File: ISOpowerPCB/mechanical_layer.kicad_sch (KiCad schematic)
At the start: 4 parts

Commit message: messing around with libraries
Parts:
- gave numbers to parts that had none: 4
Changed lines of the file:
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@@
   (symbol (lib_id "Mechanical:MountingHole") (at 71.12 78.74 0) (unit 1)
     (in_bom yes) (on_board yes) (fields_autoplaced)
-    (property "Reference" "H?" (id 0) (at 73.66 77.4699 0)
+    (property "Reference" "H4" (id 0) (at 73.66 77.4699 0)
       (effects (font (size 1.27 1.27)) (justify left))
     )
@@
   (symbol (lib_id "Mechanical:MountingHole") (at 71.12 71.12 0) (unit 1)
     (in_bom yes) (on_board yes) (fields_autoplaced)
-    (property "Reference" "H?" (id 0) (at 73.66 69.8499 0)
+    (property "Reference" "H3" (id 0) (at 73.66 69.8499 0)
       (effects (font (size 1.27 1.27)) (justify left))
     )
@@
   (symbol (lib_id "Mechanical:MountingHole") (at 71.12 62.23 0) (unit 1)
     (in_bom yes) (on_board yes) (fields_autoplaced)
-    (property "Reference" "H?" (id 0) (at 73.66 60.9599 0)
+    (property "Reference" "H2" (id 0) (at 73.66 60.9599 0)
       (effects (font (size 1.27 1.27)) (justify left))
     )
@@
   (symbol (lib_id "Mechanical:MountingHole") (at 71.12 53.34 0) (unit 1)
     (in_bom yes) (on_board yes) (fields_autoplaced)
-    (property "Reference" "H?" (id 0) (at 73.66 52.0699 0)
+    (property "Reference" "H1" (id 0) (at 73.66 52.0699 0)
       (effects (font (size 1.27 1.27)) (justify left))
     )

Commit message: Footprint Associations 50% complete
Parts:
- H1, H2, H3, H4: footprint (none) -> MountingHole:MountingHole_3.2mm_M3
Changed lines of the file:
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@@
       (effects (font (size 1.27 1.27)) (justify left))
     )
-    (property "Footprint" "" (id 2) (at 71.12 78.74 0)
+    (property "Footprint" "MountingHole:MountingHole_3.2mm_M3" (id 2) (at 71.12 78.74 0)
       (effects (font (size 1.27 1.27)) hide)
     )
@@
       (effects (font (size 1.27 1.27)) (justify left))
     )
-    (property "Footprint" "" (id 2) (at 71.12 71.12 0)
+    (property "Footprint" "MountingHole:MountingHole_3.2mm_M3" (id 2) (at 71.12 71.12 0)
       (effects (font (size 1.27 1.27)) hide)
     )
@@
       (effects (font (size 1.27 1.27)) (justify left))
     )
-    (property "Footprint" "" (id 2) (at 71.12 62.23 0)
+    (property "Footprint" "MountingHole:MountingHole_3.2mm_M3" (id 2) (at 71.12 62.23 0)
       (effects (font (size 1.27 1.27)) hide)
     )
@@
       (effects (font (size 1.27 1.27)) (justify left))
     )
-    (property "Footprint" "" (id 2) (at 71.12 53.34 0)
+    (property "Footprint" "MountingHole:MountingHole_3.2mm_M3" (id 2) (at 71.12 53.34 0)
       (effects (font (size 1.27 1.27)) hide)
     )

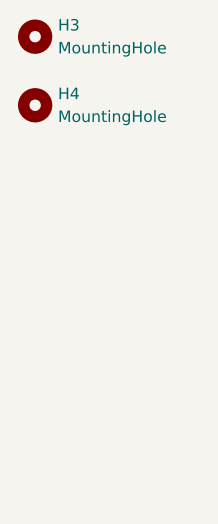
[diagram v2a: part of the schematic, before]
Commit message: Components placed V1.0
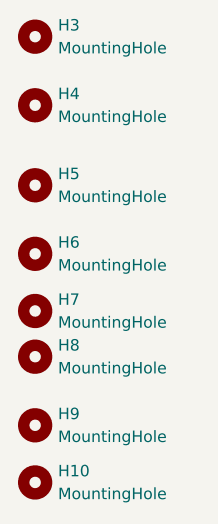
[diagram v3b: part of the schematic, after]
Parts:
- added H10, H5, H6, H7, H8, H9: MountingHole, MountingHole:MountingHole_3.2mm_M3, symbol Mechanical:MountingHole
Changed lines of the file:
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@@
 (kicad_sch (version 20211123) (generator eeschema)
   (paper "A4")
+  (symbol (lib_id "Mechanical:MountingHole") (at 71.12 120.65 0) (unit 1)
+    (in_bom yes) (on_board yes) (fields_autoplaced)
+    (property "Reference" "H10" (id 0) (at 73.66 119.3799 0)
+      (effects (font (size 1.27 1.27)) (justify left))
+    )
+    (property "Value" "MountingHole" (id 1) (at 73.66 121.9199 0)
+      (effects (font (size 1.27 1.27)) (justify left))
+    )
+    (property "Footprint" "MountingHole:MountingHole_3.2mm_M3" (id 2) (at 71.12 120.65 0)
+      (effects (font (size 1.27 1.27)) hide)
+    )
+    (property "Datasheet" "~" (id 3) (at 71.12 120.65 0)
+      (effects (font (size 1.27 1.27)) hide)
+    )
+  )
   (symbol (lib_id "Mechanical:MountingHole") (at 71.12 78.74 0) (unit 1)
     (in_bom yes) (on_board yes) (fields_autoplaced)
@@
     )
   )
+  (symbol (lib_id "Mechanical:MountingHole") (at 71.12 114.3 0) (unit 1)
+    (in_bom yes) (on_board yes) (fields_autoplaced)
+    (property "Reference" "H9" (id 0) (at 73.66 113.0299 0)
+      (effects (font (size 1.27 1.27)) (justify left))
+    )
+    (property "Value" "MountingHole" (id 1) (at 73.66 115.5699 0)
+      (effects (font (size 1.27 1.27)) (justify left))
+    )
+    (property "Footprint" "MountingHole:MountingHole_3.2mm_M3" (id 2) (at 71.12 114.3 0)
+      (effects (font (size 1.27 1.27)) hide)
+    )
+    (property "Datasheet" "~" (id 3) (at 71.12 114.3 0)
+      (effects (font (size 1.27 1.27)) hide)
+    )
+  )
+  (symbol (lib_id "Mechanical:MountingHole") (at 71.12 95.25 0) (unit 1)
+    (in_bom yes) (on_board yes) (fields_autoplaced)
+    (property "Reference" "H6" (id 0) (at 73.66 93.9799 0)
+      (effects (font (size 1.27 1.27)) (justify left))
+    )
+    (property "Value" "MountingHole" (id 1) (at 73.66 96.5199 0)
+      (effects (font (size 1.27 1.27)) (justify left))
+    )
+    (property "Footprint" "MountingHole:MountingHole_3.2mm_M3" (id 2) (at 71.12 95.25 0)
+      (effects (font (size 1.27 1.27)) hide)
+    )
+    (property "Datasheet" "~" (id 3) (at 71.12 95.25 0)
+      (effects (font (size 1.27 1.27)) hide)
+    )
+  )
   (symbol (lib_id "Mechanical:MountingHole") (at 71.12 71.12 0) (unit 1)
     (in_bom yes) (on_board yes) (fields_autoplaced)
@@
     )
     (property "Datasheet" "~" (id 3) (at 71.12 71.12 0)
+      (effects (font (size 1.27 1.27)) hide)
+    )
+  )
+  (symbol (lib_id "Mechanical:MountingHole") (at 71.12 87.63 0) (unit 1)
+    (in_bom yes) (on_board yes) (fields_autoplaced)
+    (property "Reference" "H5" (id 0) (at 73.66 86.3599 0)
+      (effects (font (size 1.27 1.27)) (justify left))
+    )
+    (property "Value" "MountingHole" (id 1) (at 73.66 88.8999 0)
+      (effects (font (size 1.27 1.27)) (justify left))
+    )
+    (property "Footprint" "MountingHole:MountingHole_3.2mm_M3" (id 2) (at 71.12 87.63 0)
+      (effects (font (size 1.27 1.27)) hide)
+    )
+    (property "Datasheet" "~" (id 3) (at 71.12 87.63 0)
       (effects (font (size 1.27 1.27)) hide)
     )
@@
       (effects (font (size 1.27 1.27)) hide)
     )
+  )
+  (symbol (lib_id "Mechanical:MountingHole") (at 71.12 101.6 0) (unit 1)
+    (in_bom yes) (on_board yes) (fields_autoplaced)
+    (property "Reference" "H7" (id 0) (at 73.66 100.3299 0)
+      (effects (font (size 1.27 1.27)) (justify left))
+    )
+    (property "Value" "MountingHole" (id 1) (at 73.66 102.8699 0)
+      (effects (font (size 1.27 1.27)) (justify left))
+    )
+    (property "Footprint" "MountingHole:MountingHole_3.2mm_M3" (id 2) (at 71.12 101.6 0)
+      (effects (font (size 1.27 1.27)) hide)
+    )
+    (property "Datasheet" "~" (id 3) (at 71.12 101.6 0)
+      (effects (font (size 1.27 1.27)) hide)
+    )
+  )
+  (symbol (lib_id "Mechanical:MountingHole") (at 71.12 106.68 0) (unit 1)
+    (in_bom yes) (on_board yes) (fields_autoplaced)
+    (property "Reference" "H8" (id 0) (at 73.66 105.4099 0)
+      (effects (font (size 1.27 1.27)) (justify left))
+    )
+    (property "Value" "MountingHole" (id 1) (at 73.66 107.9499 0)
+      (effects (font (size 1.27 1.27)) (justify left))
+    )
+    (property "Footprint" "MountingHole:MountingHole_3.2mm_M3" (id 2) (at 71.12 106.68 0)
+      (effects (font (size 1.27 1.27)) hide)
+    )
+    (property "Datasheet" "~" (id 3) (at 71.12 106.68 0)
+      (effects (font (size 1.27 1.27)) hide)
+    )

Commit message: finished PCB design. Started design review docs
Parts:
- removed H1, H2, H3, H4: MountingHole, MountingHole:MountingHole_3.2mm_M3, symbol Mechanical:MountingHole
- added H11: 2x2_ISOpower_mountingHoles, MountingHole:ISOpower_4xmounting_M3, symbol 000_Mechanical_Immo:2x2_ISOpower_mountingHoles
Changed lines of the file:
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@@
-    )
-  )
-  (symbol (lib_id "Mechanical:MountingHole") (at 71.12 78.74 0) (unit 1)
-    (in_bom yes) (on_board yes) (fields_autoplaced)
-    (property "Reference" "H4" (id 0) (at 73.66 77.4699 0)
-      (effects (font (size 1.27 1.27)) (justify left))
-    )
-    (property "Value" "MountingHole" (id 1) (at 73.66 80.0099 0)
-      (effects (font (size 1.27 1.27)) (justify left))
-    )
-    (property "Footprint" "MountingHole:MountingHole_3.2mm_M3" (id 2) (at 71.12 78.74 0)
-      (effects (font (size 1.27 1.27)) hide)
-    )
-    (property "Datasheet" "~" (id 3) (at 71.12 78.74 0)
-      (effects (font (size 1.27 1.27)) hide)
     )
   )
@@
     )
   )
-  (symbol (lib_id "Mechanical:MountingHole") (at 71.12 71.12 0) (unit 1)
-    (in_bom yes) (on_board yes) (fields_autoplaced)
-    (property "Reference" "H3" (id 0) (at 73.66 69.8499 0)
-      (effects (font (size 1.27 1.27)) (justify left))
-    )
-    (property "Value" "MountingHole" (id 1) (at 73.66 72.3899 0)
-      (effects (font (size 1.27 1.27)) (justify left))
-    )
-    (property "Footprint" "MountingHole:MountingHole_3.2mm_M3" (id 2) (at 71.12 71.12 0)
-      (effects (font (size 1.27 1.27)) hide)
-    )
-    (property "Datasheet" "~" (id 3) (at 71.12 71.12 0)
-      (effects (font (size 1.27 1.27)) hide)
-    )
-  )
   (symbol (lib_id "Mechanical:MountingHole") (at 71.12 87.63 0) (unit 1)
     (in_bom yes) (on_board yes) (fields_autoplaced)
@@
     )
   )
-  (symbol (lib_id "Mechanical:MountingHole") (at 71.12 62.23 0) (unit 1)
+  (symbol (lib_id "000_Mechanical_Immo:2x2_ISOpower_mountingHoles") (at 104.14 67.31 0) (unit 1)
     (in_bom yes) (on_board yes) (fields_autoplaced)
-    (property "Reference" "H2" (id 0) (at 73.66 60.9599 0)
+    (property "Reference" "H11" (id 0) (at 119.38 72.3899 0)
       (effects (font (size 1.27 1.27)) (justify left))
     )
-    (property "Value" "MountingHole" (id 1) (at 73.66 63.4999 0)
+    (property "Value" "2x2_ISOpower_mountingHoles" (id 1) (at 119.38 74.9299 0)
       (effects (font (size 1.27 1.27)) (justify left))
     )
-    (property "Footprint" "MountingHole:MountingHole_3.2mm_M3" (id 2) (at 71.12 62.23 0)
+    (property "Footprint" "MountingHole:ISOpower_4xmounting_M3" (id 2) (at 104.14 67.31 0)
       (effects (font (size 1.27 1.27)) hide)
     )
-    (property "Datasheet" "~" (id 3) (at 71.12 62.23 0)
+    (property "Datasheet" "~" (id 3) (at 104.14 67.31 0)
       (effects (font (size 1.27 1.27)) hide)
     )
-  )
-  (symbol (lib_id "Mechanical:MountingHole") (at 71.12 53.34 0) (unit 1)
-    (in_bom yes) (on_board yes) (fields_autoplaced)
-    (property "Reference" "H1" (id 0) (at 73.66 52.0699 0)
-      (effects (font (size 1.27 1.27)) (justify left))
-    )
-    (property "Value" "MountingHole" (id 1) (at 73.66 54.6099 0)
-      (effects (font (size 1.27 1.27)) (justify left))
-    )
-    (property "Footprint" "MountingHole:MountingHole_3.2mm_M3" (id 2) (at 71.12 53.34 0)
-      (effects (font (size 1.27 1.27)) hide)
-    )
-    (property "Datasheet" "~" (id 3) (at 71.12 53.34 0)
-      (effects (font (size 1.27 1.27)) hide)
-    )
